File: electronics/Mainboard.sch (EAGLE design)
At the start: 225 parts, among them J1 JST_PH_B3B-PH-K-S(LF)(SN), J10 JST_PH_B3B-PH-K-S(LF)(SN), J11 JST_PH_B3B-PH-K-S(LF)(SN), J12 JST_PH_B3B-PH-K-S(LF)(SN), J13 JST_PH_B3B-PH-K-S(LF)(SN), J14 JST_PH_B3B-PH-K-S(LF)(SN), J15 JST_PH_B3B-PH-K-S(LF)(SN), J16 JST_PH_B3B-PH-K-S(LF)(SN), J17 JST_PH_B3B-PH-K-S(LF)(SN), J18 JST_PH_B3B-PH-K-S(LF)(SN), J19 JST_PH_B3B-PH-K-S(LF)(SN), J2 JST_PH_B3B-PH-K-S(LF)(SN), J20 JST_PH_B3B-PH-K-S(LF)(SN), J21 JST_PH_B3B-PH-K-S(LF)(SN), J22 JST_PH_B3B-PH-K-S(LF)(SN), J23 JST_PH_B3B-PH-K-S(LF)(SN), J24 JST_PH_B3B-PH-K-S(LF)(SN), J25 JST_PH_B3B-PH-K-S(LF)(SN), J26 JST_PH_B3B-PH-K-S(LF)(SN), J27 JST_PH_B3B-PH-K-S(LF)(SN), J28 JST_PH_B3B-PH-K-S(LF)(SN), J29 JST_PH_B3B-PH-K-S(LF)(SN), J3 JST_PH_B3B-PH-K-S(LF)(SN), J30 JST_PH_B3B-PH-K-S(LF)(SN), J31 JST_PH_B3B-PH-K-S(LF)(SN), J32 JST_PH_B3B-PH-K-S(LF)(SN), J33 B4B-PH-K-S(LF)(SN), J34 B4B-PH-K-S(LF)(SN), J35 B4B-PH-K-S(LF)(SN), J36 B4B-PH-K-S(LF)(SN), J37 B4B-PH-K-S(LF)(SN), J38 B4B-PH-K-S(LF)(SN), J39 B4B-PH-K-S(LF)(SN), J4 JST_PH_B3B-PH-K-S(LF)(SN), J40 B4B-PH-K-S(LF)(SN), J41 B4B-PH-K-S(LF)(SN), J42 B4B-PH-K-S(LF)(SN), J43 B4B-PH-K-S(LF)(SN), J44 B4B-PH-K-S(LF)(SN), J45 B4B-PH-K-S(LF)(SN), J46 B4B-PH-K-S(LF)(SN), J47 B4B-PH-K-S(LF)(SN), J48 B4B-PH-K-S(LF)(SN), J49 B4B-PH-K-S(LF)(SN), J5 JST_PH_B3B-PH-K-S(LF)(SN), J50 B4B-PH-K-S(LF)(SN), J51 B4B-PH-K-S(LF)(SN), J52 B4B-PH-K-S(LF)(SN), J53 B4B-PH-K-S(LF)(SN), J54 B4B-PH-K-S(LF)(SN), J55 B4B-PH-K-S(LF)(SN), J56 B4B-PH-K-S(LF)(SN), J57 B4B-PH-K-S(LF)(SN), J58 B4B-PH-K-S(LF)(SN), J59 B4B-PH-K-S(LF)(SN), J6 JST_PH_B3B-PH-K-S(LF)(SN), J60 B4B-PH-K-S(LF)(SN), J61 B4B-PH-K-S(LF)(SN), J62 B4B-PH-K-S(LF)(SN), J63 B4B-PH-K-S(LF)(SN), J64 B4B-PH-K-S(LF)(SN), J7 JST_PH_B3B-PH-K-S(LF)(SN), J8 JST_PH_B3B-PH-K-S(LF)(SN), J9 JST_PH_B3B-PH-K-S(LF)(SN), U1 AMP-5103309-7-34PIN_5103309-7, U15 AD5360BSTZ, U16 ADR425ARZ, U18 AD7730BRUZ, U19 AD5360BSTZ, U2 AMP-5103309-7-34PIN_5103309-7, U20 ADR425ARZ, U21 AD7730BRUZ, U22 STM32F103RCT6, U23 AD7730BRUZ, U24 AD7730BRUZ, U25 AD7730BRUZ, U26 AD7730BRUZ, U27 AD7730BRUZ, U28 AD7730BRUZ, U38 AD7730BRUZ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

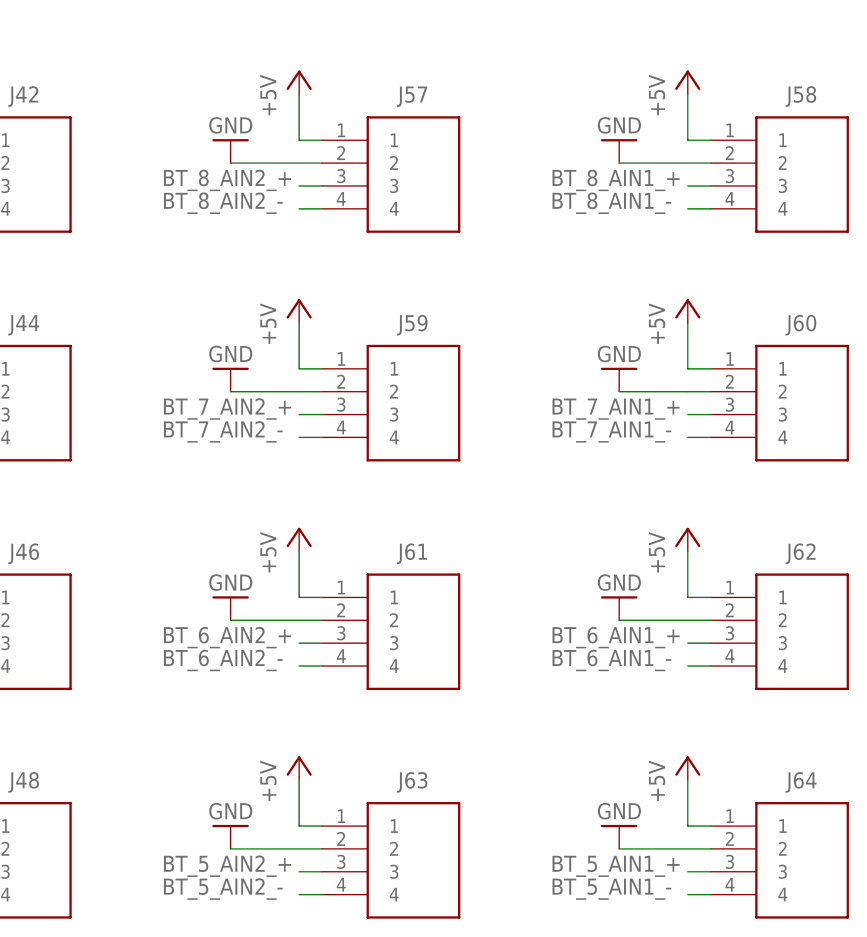
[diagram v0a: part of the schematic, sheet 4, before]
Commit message: first changes to the load cell section on the board
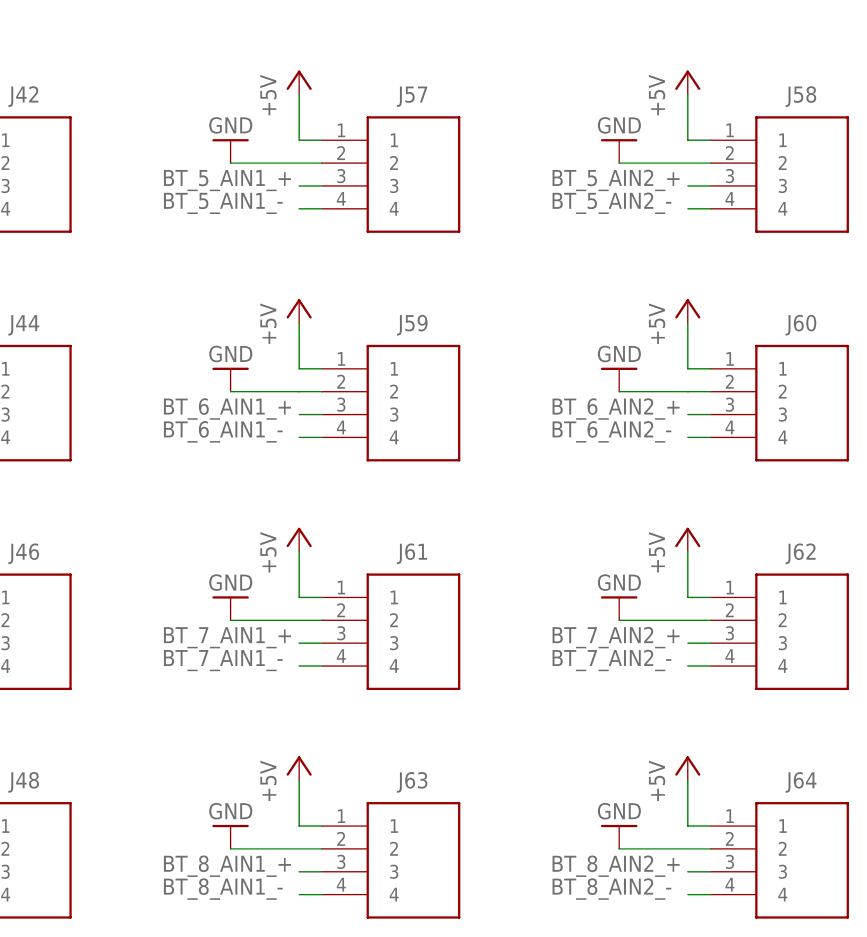
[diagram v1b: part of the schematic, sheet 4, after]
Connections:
- net N$50 renamed LC_1_OSC_IN
- net N$51 renamed LC_1_OSC_OUT
- net BT_5_AIN1_+: now also J57.3; no longer J64.3
- net BT_5_AIN1_-: now also J57.4; no longer J64.4
- net BT_5_AIN2_+: now also J58.3; no longer J63.3
- net BT_5_AIN2_-: now also J58.4; no longer J63.4
- net BT_6_AIN1_+: now also J59.3; no longer J62.3
- net BT_6_AIN1_-: now also J59.4; no longer J62.4
- net BT_6_AIN2_+: now also J60.3; no longer J61.3
- net BT_6_AIN2_-: now also J60.4; no longer J61.4
- net BT_7_AIN1_+: now also J61.3; no longer J60.3
- net BT_7_AIN1_-: now also J61.4; no longer J60.4
- net BT_7_AIN2_+: now also J62.3; no longer J59.3
- net BT_7_AIN2_-: now also J62.4; no longer J59.4
- net BT_8_AIN1_+: now also J63.3; no longer J58.3
- net BT_8_AIN1_-: now also J63.4; no longer J58.4
- net BT_8_AIN2_+: now also J64.3; no longer J57.3
- net BT_8_AIN2_-: now also J64.4; no longer J57.4
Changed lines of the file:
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@@
 </segment>
 </net>
-<net name="N$50" class="0">
+<net name="LC_1_OSC_IN" class="0">
 <segment>
 <pinref part="Y4" gate="G$1" pin="OSC1"/>
@@
 <pinref part="C18" gate="G$1" pin="1"/>
 <wire x1="228.6" y1="144.78" x2="241.3" y2="144.78" width="0.1524" layer="91"/>
+<label x="190.5" y="132.08" size="1.778" layer="95"/>
 </segment>
 </net>
-<net name="N$51" class="0">
+<net name="LC_1_OSC_OUT" class="0">
 <segment>
 <pinref part="Y4" gate="G$1" pin="OSC2"/>
@@
 <wire x1="259.08" y1="119.38" x2="259.08" y2="127" width="0.1524" layer="91"/>
 <junction x="259.08" y="127"/>
+<label x="190.5" y="129.54" size="1.778" layer="95"/>
 </segment>
 </net>
@@
 </segment>
 </net>
-<net name="BT_8_AIN2_+" class="0">
-<segment>
-<pinref part="J57" gate="G$1" pin="3"/>
-<wire x1="388.62" y1="78.74" x2="386.08" y2="78.74" width="0.1524" layer="91"/>
-<label x="370.84" y="78.74" size="1.778" layer="95"/>
-</segment>
-</net>
-<net name="BT_8_AIN2_-" class="0">
-<segment>
-<pinref part="J57" gate="G$1" pin="4"/>
-<wire x1="388.62" y1="76.2" x2="386.08" y2="76.2" width="0.1524" layer="91"/>
-<label x="370.84" y="76.2" size="1.778" layer="95"/>
-</segment>
-</net>
-<net name="BT_8_AIN1_+" class="0">
+<net name="BT_5_AIN2_+" class="0">
 <segment>
 <pinref part="J58" gate="G$1" pin="3"/>
@@
 </segment>
 </net>
-<net name="BT_8_AIN1_-" class="0">
-<segment>
-<pinref part="J58" gate="G$1" pin="4"/>
-<wire x1="431.8" y1="76.2" x2="429.26" y2="76.2" width="0.1524" layer="91"/>
-<label x="414.02" y="76.2" size="1.778" layer="95"/>
-</segment>
-</net>
-<net name="BT_7_AIN2_+" class="0">
-<segment>
-<pinref part="J59" gate="G$1" pin="3"/>
-<wire x1="388.62" y1="53.34" x2="386.08" y2="53.34" width="0.1524" layer="91"/>
-<label x="370.84" y="53.34" size="1.778" layer="95"/>
-</segment>
-</net>
-<net name="BT_7_AIN2_-" class="0">
-<segment>
-<pinref part="J59" gate="G$1" pin="4"/>
-<wire x1="388.62" y1="50.8" x2="386.08" y2="50.8" width="0.1524" layer="91"/>
-<label x="370.84" y="50.8" size="1.778" layer="95"/>
-</segment>
-</net>
-<net name="BT_7_AIN1_+" class="0">
+<net name="BT_6_AIN2_+" class="0">
 <segment>
 <pinref part="J60" gate="G$1" pin="3"/>
@@
 </segment>
 </net>
-<net name="BT_7_AIN1_-" class="0">
+<net name="BT_6_AIN2_-" class="0">
 <segment>
 <pinref part="J60" gate="G$1" pin="4"/>
@@
 </segment>
 </net>
-<net name="BT_5_AIN2_+" class="0">
-<segment>
-<pinref part="J63" gate="G$1" pin="3"/>
-<wire x1="388.62" y1="2.54" x2="386.08" y2="2.54" width="0.1524" layer="91"/>
-<label x="370.84" y="2.54" size="1.778" layer="95"/>
-</segment>
-</net>
-<net name="BT_6_AIN2_+" class="0">
-<segment>
-<pinref part="J61" gate="G$1" pin="3"/>
-<wire x1="388.62" y1="27.94" x2="386.08" y2="27.94" width="0.1524" layer="91"/>
-<label x="370.84" y="27.94" size="1.778" layer="95"/>
-</segment>
-</net>
-<net name="BT_6_AIN2_-" class="0">
-<segment>
-<pinref part="J61" gate="G$1" pin="4"/>
-<wire x1="388.62" y1="25.4" x2="386.08" y2="25.4" width="0.1524" layer="91"/>
-<label x="370.84" y="25.4" size="1.778" layer="95"/>
-</segment>
-</net>
 <net name="BT_6_AIN1_+" class="0">
 <segment>
-<pinref part="J62" gate="G$1" pin="3"/>
-<wire x1="431.8" y1="27.94" x2="429.26" y2="27.94" width="0.1524" layer="91"/>
-<label x="414.02" y="27.94" size="1.778" layer="95"/>
+<pinref part="J59" gate="G$1" pin="3"/>
+<wire x1="388.62" y1="53.34" x2="386.08" y2="53.34" width="0.1524" layer="91"/>
+<label x="370.84" y="53.34" size="1.778" layer="95"/>
 </segment>
 </net>
 <net name="BT_6_AIN1_-" class="0">
 <segment>
-<pinref part="J62" gate="G$1" pin="4"/>
-<wire x1="431.8" y1="25.4" x2="429.26" y2="25.4" width="0.1524" layer="91"/>
-<label x="414.02" y="25.4" size="1.778" layer="95"/>
+<pinref part="J59" gate="G$1" pin="4"/>
+<wire x1="388.62" y1="50.8" x2="386.08" y2="50.8" width="0.1524" layer="91"/>
+<label x="370.84" y="50.8" size="1.778" layer="95"/>
 </segment>
 </net>
 <net name="BT_5_AIN1_+" class="0">
 <segment>
-<pinref part="J64" gate="G$1" pin="3"/>
-<wire x1="431.8" y1="2.54" x2="429.26" y2="2.54" width="0.1524" layer="91"/>
-<label x="414.02" y="2.54" size="1.778" layer="95"/>
+<pinref part="J57" gate="G$1" pin="3"/>
+<wire x1="388.62" y1="78.74" x2="386.08" y2="78.74" width="0.1524" layer="91"/>
+<label x="370.84" y="78.74" size="1.778" layer="95"/>
 </segment>
 </net>
 <net name="BT_5_AIN1_-" class="0">
 <segment>
-<pinref part="J64" gate="G$1" pin="4"/>
-<wire x1="431.8" y1="0" x2="429.26" y2="0" width="0.1524" layer="91"/>
-<label x="414.02" y="0" size="1.778" layer="95"/>
+<pinref part="J57" gate="G$1" pin="4"/>
+<wire x1="388.62" y1="76.2" x2="386.08" y2="76.2" width="0.1524" layer="91"/>
+<label x="370.84" y="76.2" size="1.778" layer="95"/>
 </segment>
 </net>
 <net name="BT_5_AIN2_-" class="0">
 <segment>
-<pinref part="J63" gate="G$1" pin="4"/>
-<wire x1="388.62" y1="0" x2="386.08" y2="0" width="0.1524" layer="91"/>
-<label x="370.84" y="0" size="1.778" layer="95"/>
+<pinref part="J58" gate="G$1" pin="4"/>
+<wire x1="431.8" y1="76.2" x2="429.26" y2="76.2" width="0.1524" layer="91"/>
+<label x="414.02" y="76.2" size="1.778" layer="95"/>
 </segment>
 </net>
@@
 </segment>
 </net>
+<net name="BT_7_AIN1_+" class="0">
+<segment>
+<pinref part="J61" gate="G$1" pin="3"/>
+<wire x1="388.62" y1="27.94" x2="386.08" y2="27.94" width="0.1524" layer="91"/>
+<label x="370.84" y="27.94" size="1.778" layer="95"/>
+</segment>
+</net>
+<net name="BT_7_AIN1_-" class="0">
+<segment>
+<pinref part="J61" gate="G$1" pin="4"/>
+<wire x1="388.62" y1="25.4" x2="386.08" y2="25.4" width="0.1524" layer="91"/>
+<label x="370.84" y="25.4" size="1.778" layer="95"/>
+</segment>
+</net>
+<net name="BT_7_AIN2_+" class="0">
+<segment>
+<pinref part="J62" gate="G$1" pin="3"/>
+<wire x1="431.8" y1="27.94" x2="429.26" y2="27.94" width="0.1524" layer="91"/>
+<label x="414.02" y="27.94" size="1.778" layer="95"/>
+</segment>
+</net>
+<net name="BT_7_AIN2_-" class="0">
+<segment>
+<pinref part="J62" gate="G$1" pin="4"/>
+<wire x1="431.8" y1="25.4" x2="429.26" y2="25.4" width="0.1524" layer="91"/>
+<label x="414.02" y="25.4" size="1.778" layer="95"/>
+</segment>
+</net>
+<net name="BT_8_AIN1_+" class="0">
+<segment>
+<pinref part="J63" gate="G$1" pin="3"/>
+<wire x1="388.62" y1="2.54" x2="386.08" y2="2.54" width="0.1524" layer="91"/>
+<label x="370.84" y="2.54" size="1.778" layer="95"/>
+</segment>
+</net>
+<net name="BT_8_AIN1_-" class="0">
+<segment>
+<pinref part="J63" gate="G$1" pin="4"/>
+<wire x1="388.62" y1="0" x2="386.08" y2="0" width="0.1524" layer="91"/>
+<label x="370.84" y="0" size="1.778" layer="95"/>
+</segment>
+</net>
+<net name="BT_8_AIN2_+" class="0">
+<segment>
+<pinref part="J64" gate="G$1" pin="3"/>
+<wire x1="431.8" y1="2.54" x2="429.26" y2="2.54" width="0.1524" layer="91"/>
+<label x="414.02" y="2.54" size="1.778" layer="95"/>
+</segment>
+</net>
+<net name="BT_8_AIN2_-" class="0">
+<segment>
+<pinref part="J64" gate="G$1" pin="4"/>
+<wire x1="431.8" y1="0" x2="429.26" y2="0" width="0.1524" layer="91"/>
+<label x="414.02" y="0" size="1.778" layer="95"/>
+</segment>
+</net>
